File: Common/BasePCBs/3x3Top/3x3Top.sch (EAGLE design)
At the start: 2 parts

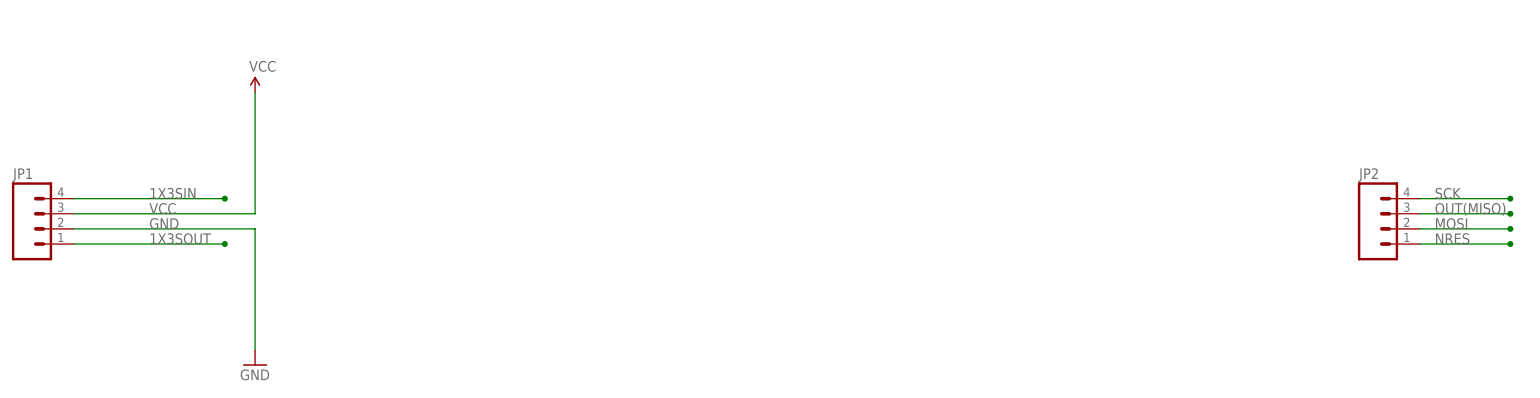
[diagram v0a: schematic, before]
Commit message: Added programmable module's top PCB
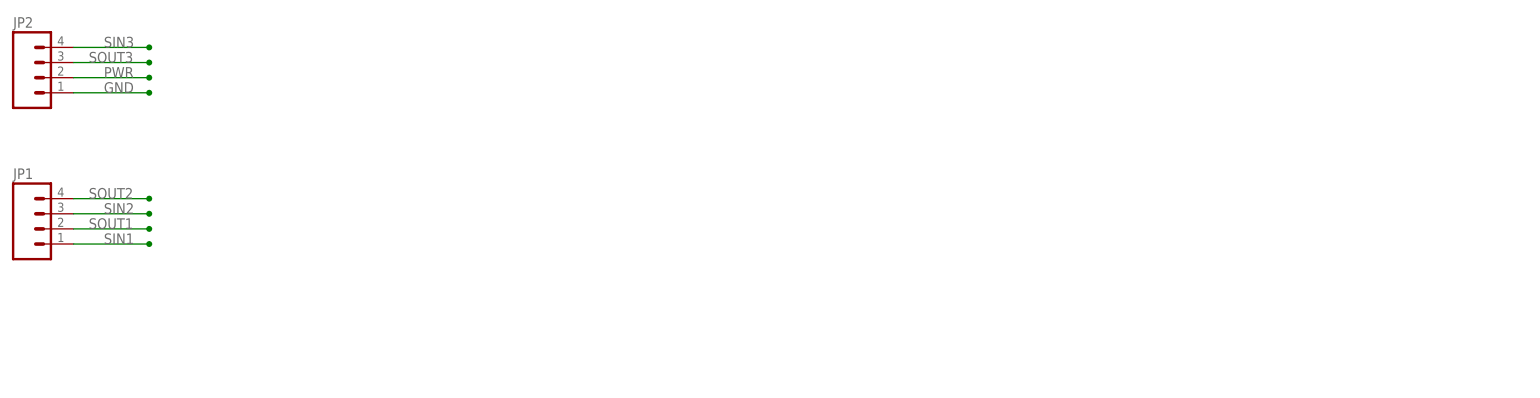
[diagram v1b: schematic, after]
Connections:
- net 1X3SIN renamed SOUT2
- net 1X3SOUT renamed SIN1
- net MOSI renamed PWR
- net OUT(MISO) renamed SOUT3
- net SCK renamed SIN3
- net VCC renamed SIN2
- removed net NRES: JP2.1
- new net SOUT1: JP1.2
- net GND: now also JP2.1; no longer JP1.2
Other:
- moved on the sheet: JP2
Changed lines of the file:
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@@
 <layers>
 <layer number="1" name="Top" color="4" fill="1" visible="no" active="no"/>
-<layer number="2" name="Route2" color="1" fill="3" visible="no" active="no"/>
-<layer number="15" name="Route15" color="4" fill="6" visible="no" active="no"/>
 <layer number="16" name="Bottom" color="1" fill="1" visible="no" active="no"/>
 <layer number="17" name="Pads" color="2" fill="1" visible="no" active="no"/>
@@
 <parts>
 <part name="JP1" library="SparkFun-Connectors" deviceset="M04" device="PTH"/>
-<part name="SUPPLY1" library="SparkFun-Aesthetics" deviceset="VCC" device=""/>
-<part name="GND1" library="SparkFun-Aesthetics" deviceset="GND" device=""/>
 <part name="JP2" library="SparkFun-Connectors" deviceset="M04" device="PTH"/>
 </parts>
@@
 <instances>
 <instance part="JP1" gate="G$1" x="5.08" y="5.08"/>
-<instance part="SUPPLY1" gate="G$1" x="40.64" y="27.94"/>
-<instance part="GND1" gate="1" x="40.64" y="-17.78"/>
-<instance part="JP2" gate="G$1" x="231.14" y="5.08"/>
+<instance part="JP2" gate="G$1" x="5.08" y="30.48"/>
 </instances>
 <busses>
 </busses>
 <nets>
-<net name="1X3SIN" class="0">
+<net name="SIN3" class="0">
+<segment>
+<pinref part="JP2" gate="G$1" pin="4"/>
+<wire x1="10.16" y1="35.56" x2="22.86" y2="35.56" width="0.1524" layer="91"/>
+<junction x="22.86" y="35.56"/>
+<label x="15.24" y="35.56" size="1.778" layer="95"/>
+</segment>
+</net>
+<net name="SOUT3" class="0">
+<segment>
+<pinref part="JP2" gate="G$1" pin="3"/>
+<wire x1="10.16" y1="33.02" x2="22.86" y2="33.02" width="0.1524" layer="91"/>
+<junction x="22.86" y="33.02"/>
+<label x="12.7" y="33.02" size="1.778" layer="95"/>
+</segment>
+</net>
+<net name="PWR" class="0">
+<segment>
+<pinref part="JP2" gate="G$1" pin="2"/>
+<wire x1="10.16" y1="30.48" x2="22.86" y2="30.48" width="0.1524" layer="91"/>
+<junction x="22.86" y="30.48"/>
+<label x="15.24" y="30.48" size="1.778" layer="95"/>
+</segment>
+</net>
+<net name="GND" class="0">
+<segment>
+<pinref part="JP2" gate="G$1" pin="1"/>
+<wire x1="10.16" y1="27.94" x2="22.86" y2="27.94" width="0.1524" layer="91"/>
+<junction x="22.86" y="27.94"/>
+<label x="15.24" y="27.94" size="1.778" layer="95"/>
+</segment>
+</net>
+<net name="SOUT2" class="0">
 <segment>
 <pinref part="JP1" gate="G$1" pin="4"/>
-<wire x1="10.16" y1="10.16" x2="35.56" y2="10.16" width="0.1524" layer="91"/>
-<label x="22.86" y="10.16" size="1.778" layer="95"/>
-<junction x="35.56" y="10.16"/>
-</segment>
-</net>
-<net name="VCC" class="0">
+<wire x1="10.16" y1="10.16" x2="22.86" y2="10.16" width="0.1524" layer="91"/>
+<junction x="22.86" y="10.16"/>
+<label x="12.7" y="10.16" size="1.778" layer="95"/>
+</segment>
+</net>
+<net name="SIN2" class="0">
 <segment>
 <pinref part="JP1" gate="G$1" pin="3"/>
-<wire x1="10.16" y1="7.62" x2="40.64" y2="7.62" width="0.1524" layer="91"/>
-<label x="22.86" y="7.62" size="1.778" layer="95"/>
-<pinref part="SUPPLY1" gate="G$1" pin="VCC"/>
-<wire x1="40.64" y1="7.62" x2="40.64" y2="27.94" width="0.1524" layer="91"/>
-</segment>
-</net>
-<net name="GND" class="0">
+<wire x1="10.16" y1="7.62" x2="22.86" y2="7.62" width="0.1524" layer="91"/>
+<junction x="22.86" y="7.62"/>
+<label x="15.24" y="7.62" size="1.778" layer="95"/>
+</segment>
+</net>
+<net name="SOUT1" class="0">
 <segment>
 <pinref part="JP1" gate="G$1" pin="2"/>
-<wire x1="10.16" y1="5.08" x2="40.64" y2="5.08" width="0.1524" layer="91"/>
-<label x="22.86" y="5.08" size="1.778" layer="95"/>
-<pinref part="GND1" gate="1" pin="GND"/>
-<wire x1="40.64" y1="5.08" x2="40.64" y2="-15.24" width="0.1524" layer="91"/>
-</segment>
-</net>
-<net name="1X3SOUT" class="0">
+<wire x1="10.16" y1="5.08" x2="22.86" y2="5.08" width="0.1524" layer="91"/>
+<junction x="22.86" y="5.08"/>
+<label x="12.7" y="5.08" size="1.778" layer="95"/>
+</segment>
+</net>
+<net name="SIN1" class="0">
 <segment>
 <pinref part="JP1" gate="G$1" pin="1"/>
-<wire x1="10.16" y1="2.54" x2="35.56" y2="2.54" width="0.1524" layer="91"/>
-<label x="22.86" y="2.54" size="1.778" layer="95"/>
-<junction x="35.56" y="2.54"/>
-</segment>
-</net>
-<net name="OUT(MISO)" class="0">
-<segment>
-<pinref part="JP2" gate="G$1" pin="3"/>
-<label x="238.76" y="7.62" size="1.778" layer="95"/>
-<wire x1="236.22" y1="7.62" x2="251.46" y2="7.62" width="0.1524" layer="91"/>
-<junction x="251.46" y="7.62"/>
-</segment>
-</net>
-<net name="MOSI" class="0">
-<segment>
-<pinref part="JP2" gate="G$1" pin="2"/>
-<label x="238.76" y="5.08" size="1.778" layer="95"/>
-<wire x1="236.22" y1="5.08" x2="251.46" y2="5.08" width="0.1524" layer="91"/>
-<junction x="251.46" y="5.08"/>
-</segment>
-</net>
-<net name="SCK" class="0">
-<segment>
-<pinref part="JP2" gate="G$1" pin="4"/>
-<label x="238.76" y="10.16" size="1.778" layer="95"/>
-<wire x1="236.22" y1="10.16" x2="251.46" y2="10.16" width="0.1524" layer="91"/>
-<junction x="251.46" y="10.16"/>
-</segment>
-</net>
-<net name="NRES" class="0">
-<segment>
-<pinref part="JP2" gate="G$1" pin="1"/>
-<label x="238.76" y="2.54" size="1.778" layer="95"/>
-<wire x1="236.22" y1="2.54" x2="251.46" y2="2.54" width="0.1524" layer="91"/>
-<junction x="251.46" y="2.54"/>
-</segment>
-</net>
+<wire x1="10.16" y1="2.54" x2="22.86" y2="2.54" width="0.1524" layer="91"/>
+<junction x="22.86" y="2.54"/>
+<label x="15.24" y="2.54" size="1.778" layer="95"/>
+</segment>
+</net>
